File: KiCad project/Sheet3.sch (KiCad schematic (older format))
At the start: 5 parts, among them U3 MPU-9150

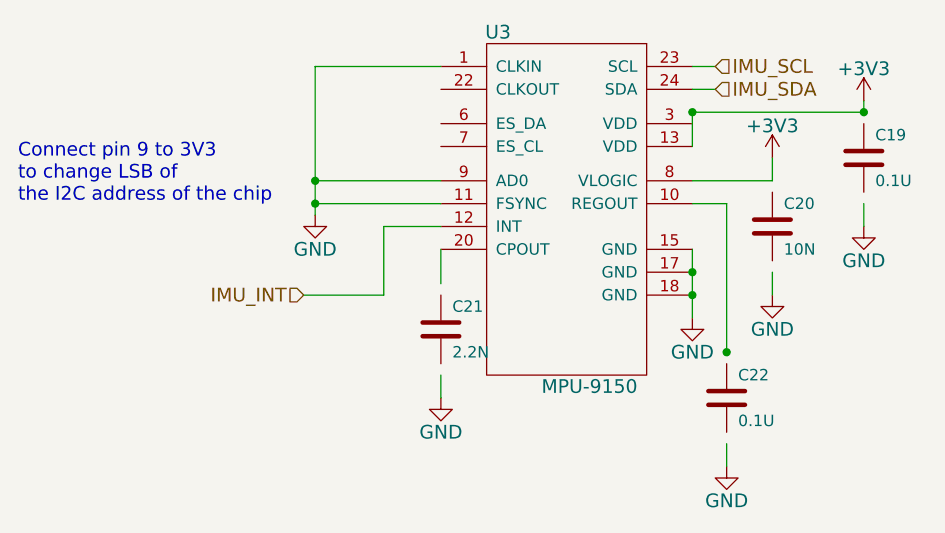
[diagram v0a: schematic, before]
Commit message: IC packages, bugfixes
drawings for IC packages, associations, schematic fixes
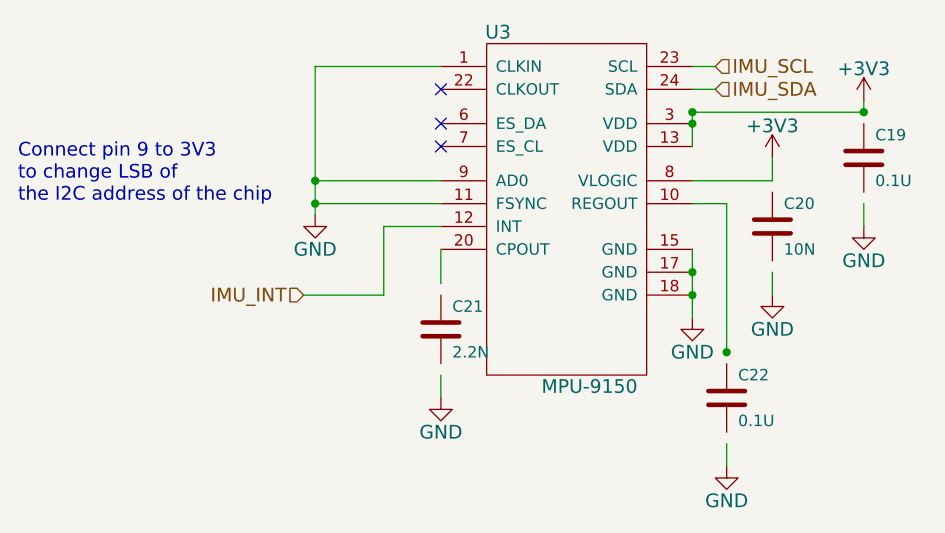
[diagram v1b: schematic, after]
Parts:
- U3: footprint (none) -> Anastasia:LGA24
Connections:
- no-connect marks 0 -> 3
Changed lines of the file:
@@
 $Descr A4 11693 8268
 encoding utf-8
-Sheet 4 7
+Sheet 4 10
 Title "IMU MPU-9150"
 Date "15 March 2015"
@@
 $EndDescr
 $Comp
-L +3V3 #PWR17
+L +3V3 #PWR020
 U 1 1 5504DED0
 P 4750 1000
-F 0 "#PWR17" H 4750 850 60  0001 C CNN
+F 0 "#PWR020" H 4750 850 60  0001 C CNN
 F 1 "+3V3" H 4750 1140 60  0000 C CNN
 F 2 "" H 4750 1000 60  0000 C CNN
@@
 $EndComp
 $Comp
-L GND #PWR20
+L GND #PWR021
 U 1 1 5504DEF3
 P 4750 1550
-F 0 "#PWR20" H 4750 1300 60  0001 C CNN
+F 0 "#PWR021" H 4750 1300 60  0001 C CNN
 F 1 "GND" H 4750 1400 60  0000 C CNN
 F 2 "" H 4750 1550 60  0000 C CNN
@@
 F 0 "C20" H 4400 1650 50  0000 L CNN
 F 1 "10N" H 4400 1450 50  0000 L CNN
-F 2 "" H 4388 1400 30  0000 C CNN
+F 2 "" H 4388 1400 30  0001 C CNN
 F 3 "" H 4350 1550 60  0000 C CNN
 	1    4350 1550
@@
 F 0 "U3" H 3150 800 60  0000 C CNN
 F 1 "MPU-9150" H 3550 -750 60  0000 C CNN
-F 2 "" H 3100 750 60  0000 C CNN
+F 2 "Anastasia:LGA24" H 3100 750 60  0001 C CNN
 F 3 "" H 3100 750 60  0000 C CNN
 	1    3100 750
@@
 F 0 "C22" H 4200 2400 50  0000 L CNN
 F 1 "0.1U" H 4200 2200 50  0000 L CNN
-F 2 "" H 4188 2150 30  0000 C CNN
+F 2 "" H 4188 2150 30  0001 C CNN
 F 3 "" H 4150 2300 60  0000 C CNN
 	1    4150 2300
@@
 F 0 "C19" H 4800 1350 50  0000 L CNN
 F 1 "0.1U" H 4800 1150 50  0000 L CNN
-F 2 "" H 4788 1100 30  0000 C CNN
+F 2 "" H 4788 1100 30  0001 C CNN
 F 3 "" H 4750 1250 60  0000 C CNN
 	1    4750 1250
@@
 	4000 1050 4750 1050
 $Comp
-L +3V3 #PWR18
+L +3V3 #PWR022
 U 1 1 5504E385
 P 4350 1250
-F 0 "#PWR18" H 4350 1100 60  0001 C CNN
+F 0 "#PWR022" H 4350 1100 60  0001 C CNN
 F 1 "+3V3" H 4350 1390 60  0000 C CNN
 F 2 "" H 4350 1250 60  0000 C CNN
@@
 	4350 1250 4350 1350
 $Comp
-L GND #PWR21
+L GND #PWR023
 U 1 1 5504E3C5
 P 4350 1850
-F 0 "#PWR21" H 4350 1600 60  0001 C CNN
+F 0 "#PWR023" H 4350 1600 60  0001 C CNN
 F 1 "GND" H 4350 1700 60  0000 C CNN
 F 2 "" H 4350 1850 60  0000 C CNN
@@
 $EndComp
 $Comp
-L GND #PWR24
+L GND #PWR024
 U 1 1 5504E3EC
 P 4150 2600
-F 0 "#PWR24" H 4150 2350 60  0001 C CNN
+F 0 "#PWR024" H 4150 2350 60  0001 C CNN
 F 1 "GND" H 4150 2450 60  0000 C CNN
 F 2 "" H 4150 2600 60  0000 C CNN
@@
 	4150 2500 4150 2600
 $Comp
-L GND #PWR22
+L GND #PWR025
 U 1 1 5504E44A
 P 4000 1950
-F 0 "#PWR22" H 4000 1700 60  0001 C CNN
+F 0 "#PWR025" H 4000 1700 60  0001 C CNN
 F 1 "GND" H 4000 1800 60  0000 C CNN
 F 2 "" H 4000 1950 60  0000 C CNN
@@
 F 0 "C21" H 2950 2100 50  0000 L CNN
 F 1 "2.2N" H 2950 1900 50  0000 L CNN
-F 2 "" H 2938 1850 30  0000 C CNN
+F 2 "" H 2938 1850 30  0001 C CNN
 F 3 "" H 2900 2000 60  0000 C CNN
 	1    2900 2000
@@
 $EndComp
 $Comp
-L GND #PWR23
+L GND #PWR026
 U 1 1 5504E498
 P 2900 2300
-F 0 "#PWR23" H 2900 2050 60  0001 C CNN
+F 0 "#PWR026" H 2900 2050 60  0001 C CNN
 F 1 "GND" H 2900 2150 60  0000 C CNN
 F 2 "" H 2900 2300 60  0000 C CNN
@@
 	2900 2200 2900 2300
 $Comp
-L GND #PWR19
+L GND #PWR027
 U 1 1 550533AC
 P 2350 1500
-F 0 "#PWR19" H 2350 1250 60  0001 C CNN
+F 0 "#PWR027" H 2350 1250 60  0001 C CNN
 F 1 "GND" H 2350 1350 60  0000 C CNN
 F 2 "" H 2350 1500 60  0000 C CNN
@@
 Wire Wire Line
 	2650 1850 2300 1850
+Connection ~ 4000 1100
+NoConn ~ 2900 1200
+NoConn ~ 2900 1100
+NoConn ~ 2900 950
 $EndSCHEMATC

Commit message: New packages, PCB
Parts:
- C20: renamed from C19; footprint (none) -> Capacitors_SMD:C_0603
- C21: renamed from C20; footprint (none) -> Capacitors_SMD:C_0603
- C22: renamed from C21; footprint (none) -> Capacitors_SMD:C_0603
- C23: renamed from C22; footprint (none) -> Capacitors_SMD:C_0603
- renumbered U3 to U5
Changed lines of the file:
@@
 $EndDescr
 $Comp
-L +3V3 #PWR020
+L +3V3 #PWR019
 U 1 1 5504DED0
 P 4750 1000
-F 0 "#PWR020" H 4750 850 60  0001 C CNN
+F 0 "#PWR019" H 4750 850 60  0001 C CNN
 F 1 "+3V3" H 4750 1140 60  0000 C CNN
 F 2 "" H 4750 1000 60  0000 C CNN
@@
 $EndComp
 $Comp
-L GND #PWR021
+L GND #PWR020
 U 1 1 5504DEF3
 P 4750 1550
-F 0 "#PWR021" H 4750 1300 60  0001 C CNN
+F 0 "#PWR020" H 4750 1300 60  0001 C CNN
 F 1 "GND" H 4750 1400 60  0000 C CNN
 F 2 "" H 4750 1550 60  0000 C CNN
@@
 $EndComp
 $Comp
-L C C20
+L C C21
 U 1 1 5504DF2D
 P 4350 1550
-F 0 "C20" H 4400 1650 50  0000 L CNN
+F 0 "C21" H 4400 1650 50  0000 L CNN
 F 1 "10N" H 4400 1450 50  0000 L CNN
-F 2 "" H 4388 1400 30  0001 C CNN
+F 2 "Capacitors_SMD:C_0603" H 4388 1400 30  0001 C CNN
 F 3 "" H 4350 1550 60  0000 C CNN
 	1    4350 1550
@@
 $EndComp
 $Comp
-L MPU-9150 U3
+L MPU-9150 U5
 U 1 1 5504E110
 P 3100 750
-F 0 "U3" H 3150 800 60  0000 C CNN
+F 0 "U5" H 3150 800 60  0000 C CNN
 F 1 "MPU-9150" H 3550 -750 60  0000 C CNN
 F 2 "Anastasia:LGA24" H 3100 750 60  0001 C CNN
@@
 	4150 1450 4150 2100
 $Comp
-L C C22
+L C C23
 U 1 1 5504E266
 P 4150 2300
-F 0 "C22" H 4200 2400 50  0000 L CNN
+F 0 "C23" H 4200 2400 50  0000 L CNN
 F 1 "0.1U" H 4200 2200 50  0000 L CNN
-F 2 "" H 4188 2150 30  0001 C CNN
+F 2 "Capacitors_SMD:C_0603" H 4188 2150 30  0001 C CNN
 F 3 "" H 4150 2300 60  0000 C CNN
 	1    4150 2300
@@
 Connection ~ 4150 2100
 $Comp
-L C C19
+L C C20
 U 1 1 5504E2C2
 P 4750 1250
-F 0 "C19" H 4800 1350 50  0000 L CNN
+F 0 "C20" H 4800 1350 50  0000 L CNN
 F 1 "0.1U" H 4800 1150 50  0000 L CNN
-F 2 "" H 4788 1100 30  0001 C CNN
+F 2 "Capacitors_SMD:C_0603" H 4788 1100 30  0001 C CNN
 F 3 "" H 4750 1250 60  0000 C CNN
 	1    4750 1250
@@
 	4000 1050 4750 1050
 $Comp
-L +3V3 #PWR022
+L +3V3 #PWR021
 U 1 1 5504E385
 P 4350 1250
-F 0 "#PWR022" H 4350 1100 60  0001 C CNN
+F 0 "#PWR021" H 4350 1100 60  0001 C CNN
 F 1 "+3V3" H 4350 1390 60  0000 C CNN
 F 2 "" H 4350 1250 60  0000 C CNN
@@
 	4350 1250 4350 1350
 $Comp
-L GND #PWR023
+L GND #PWR022
 U 1 1 5504E3C5
 P 4350 1850
-F 0 "#PWR023" H 4350 1600 60  0001 C CNN
+F 0 "#PWR022" H 4350 1600 60  0001 C CNN
 F 1 "GND" H 4350 1700 60  0000 C CNN
 F 2 "" H 4350 1850 60  0000 C CNN
@@
 $EndComp
 $Comp
-L GND #PWR024
+L GND #PWR023
 U 1 1 5504E3EC
 P 4150 2600
-F 0 "#PWR024" H 4150 2350 60  0001 C CNN
+F 0 "#PWR023" H 4150 2350 60  0001 C CNN
 F 1 "GND" H 4150 2450 60  0000 C CNN
 F 2 "" H 4150 2600 60  0000 C CNN
@@
 	4150 2500 4150 2600
 $Comp
-L GND #PWR025
+L GND #PWR024
 U 1 1 5504E44A
 P 4000 1950
-F 0 "#PWR025" H 4000 1700 60  0001 C CNN
+F 0 "#PWR024" H 4000 1700 60  0001 C CNN
 F 1 "GND" H 4000 1800 60  0000 C CNN
 F 2 "" H 4000 1950 60  0000 C CNN
@@
 Connection ~ 4000 1850
 $Comp
-L C C21
+L C C22
 U 1 1 5504E476
 P 2900 2000
-F 0 "C21" H 2950 2100 50  0000 L CNN
+F 0 "C22" H 2950 2100 50  0000 L CNN
 F 1 "2.2N" H 2950 1900 50  0000 L CNN
-F 2 "" H 2938 1850 30  0001 C CNN
+F 2 "Capacitors_SMD:C_0603" H 2938 1850 30  0001 C CNN
 F 3 "" H 2900 2000 60  0000 C CNN
 	1    2900 2000
@@
 $EndComp
 $Comp
-L GND #PWR026
+L GND #PWR025
 U 1 1 5504E498
 P 2900 2300
-F 0 "#PWR026" H 2900 2050 60  0001 C CNN
+F 0 "#PWR025" H 2900 2050 60  0001 C CNN
 F 1 "GND" H 2900 2150 60  0000 C CNN
 F 2 "" H 2900 2300 60  0000 C CNN
@@
 	2900 2200 2900 2300
 $Comp
-L GND #PWR027
+L GND #PWR026
 U 1 1 550533AC
 P 2350 1500
-F 0 "#PWR027" H 2350 1250 60  0001 C CNN
+F 0 "#PWR026" H 2350 1250 60  0001 C CNN
 F 1 "GND" H 2350 1350 60  0000 C CNN
 F 2 "" H 2350 1500 60  0000 C CNN

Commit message: Refactoring
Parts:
- C20, C23: value 0.1U -> 100N
- U5: value MPU-9150 -> MPU-9250
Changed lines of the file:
@@
 LIBS:memory
 LIBS:xilinx
-LIBS:special
 LIBS:microcontrollers
 LIBS:dsp
@@
 U 1 1 5504DF2D
 P 4350 1550
+AR Path="/5504DF2D" Ref="C21"  Part="1"
+AR Path="/5504DA44/5504DF2D" Ref="C21"  Part="1"
 F 0 "C21" H 4400 1650 50  0000 L CNN
 F 1 "10N" H 4400 1450 50  0000 L CNN
@@
 P 3100 750
 F 0 "U5" H 3150 800 60  0000 C CNN
-F 1 "MPU-9150" H 3550 -750 60  0000 C CNN
+F 1 "MPU-9250" H 3550 -750 60  0000 C CNN
 F 2 "Anastasia:LGA24" H 3100 750 60  0001 C CNN
 F 3 "" H 3100 750 60  0000 C CNN
@@
 	4000 1050 4000 1200
 Wire Wire Line
-	4750 1050 4750 1000
+	4750 1000 4750 1100
 Connection ~ 4000 1050
 Connection ~ 4750 1050
@@
 	4000 1450 4150 1450
 Wire Wire Line
-	4150 1450 4150 2100
+	4150 1450 4150 2150
 $Comp
 L C C23
 U 1 1 5504E266
 P 4150 2300
+AR Path="/5504E266" Ref="C23"  Part="1"
+AR Path="/5504DA44/5504E266" Ref="C23"  Part="1"
 F 0 "C23" H 4200 2400 50  0000 L CNN
-F 1 "0.1U" H 4200 2200 50  0000 L CNN
+F 1 "100N" H 4200 2200 50  0000 L CNN
 F 2 "Capacitors_SMD:C_0603" H 4188 2150 30  0001 C CNN
 F 3 "" H 4150 2300 60  0000 C CNN
@@
 U 1 1 5504E2C2
 P 4750 1250
+AR Path="/5504E2C2" Ref="C20"  Part="1"
+AR Path="/5504DA44/5504E2C2" Ref="C20"  Part="1"
 F 0 "C20" H 4800 1350 50  0000 L CNN
-F 1 "0.1U" H 4800 1150 50  0000 L CNN
+F 1 "100N" H 4800 1150 50  0000 L CNN
 F 2 "Capacitors_SMD:C_0603" H 4788 1100 30  0001 C CNN
 F 3 "" H 4750 1250 60  0000 C CNN
@@
 $EndComp
 Wire Wire Line
-	4750 1450 4750 1550
+	4750 1400 4750 1550
 Wire Wire Line
 	4000 1050 4750 1050
@@
 $EndComp
 Wire Wire Line
-	4350 1250 4350 1350
+	4350 1250 4350 1400
 $Comp
 L GND #PWR07
@@
 $EndComp
 Wire Wire Line
-	4350 1750 4350 1850
-Wire Wire Line
-	4150 2500 4150 2600
+	4350 1700 4350 1850
+Wire Wire Line
+	4150 2450 4150 2600
 $Comp
 L GND #PWR09
@@
 U 1 1 5504E476
 P 2900 2000
+AR Path="/5504E476" Ref="C22"  Part="1"
+AR Path="/5504DA44/5504E476" Ref="C22"  Part="1"
 F 0 "C22" H 2950 2100 50  0000 L CNN
 F 1 "2.2N" H 2950 1900 50  0000 L CNN
@@
 $EndComp
 Wire Wire Line
-	2900 1650 2900 1800
-Wire Wire Line
-	2900 2200 2900 2300
+	2900 1650 2900 1850
+Wire Wire Line
+	2900 2150 2900 2300
 $Comp
 L GND #PWR011
@@
 NoConn ~ 2900 1100
 NoConn ~ 2900 950
+Connection ~ 4350 1350
 $EndSCHEMATC
